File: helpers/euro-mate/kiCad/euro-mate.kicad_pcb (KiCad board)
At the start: 2 copper layers, 41 parts, among them J1 PWR, J10 OUT_2, J11 OUT_3, J12 OUT_4, J13 Conn_01x04, J14 Conn_01x04, J2 BB_TOP_RAIL, J2 PWR, J3 BB_BTM_RAIL, J5 JACK_1, J6 JACK_2, J7 JACK_3, J8 JACK_4, J9 OUT_1

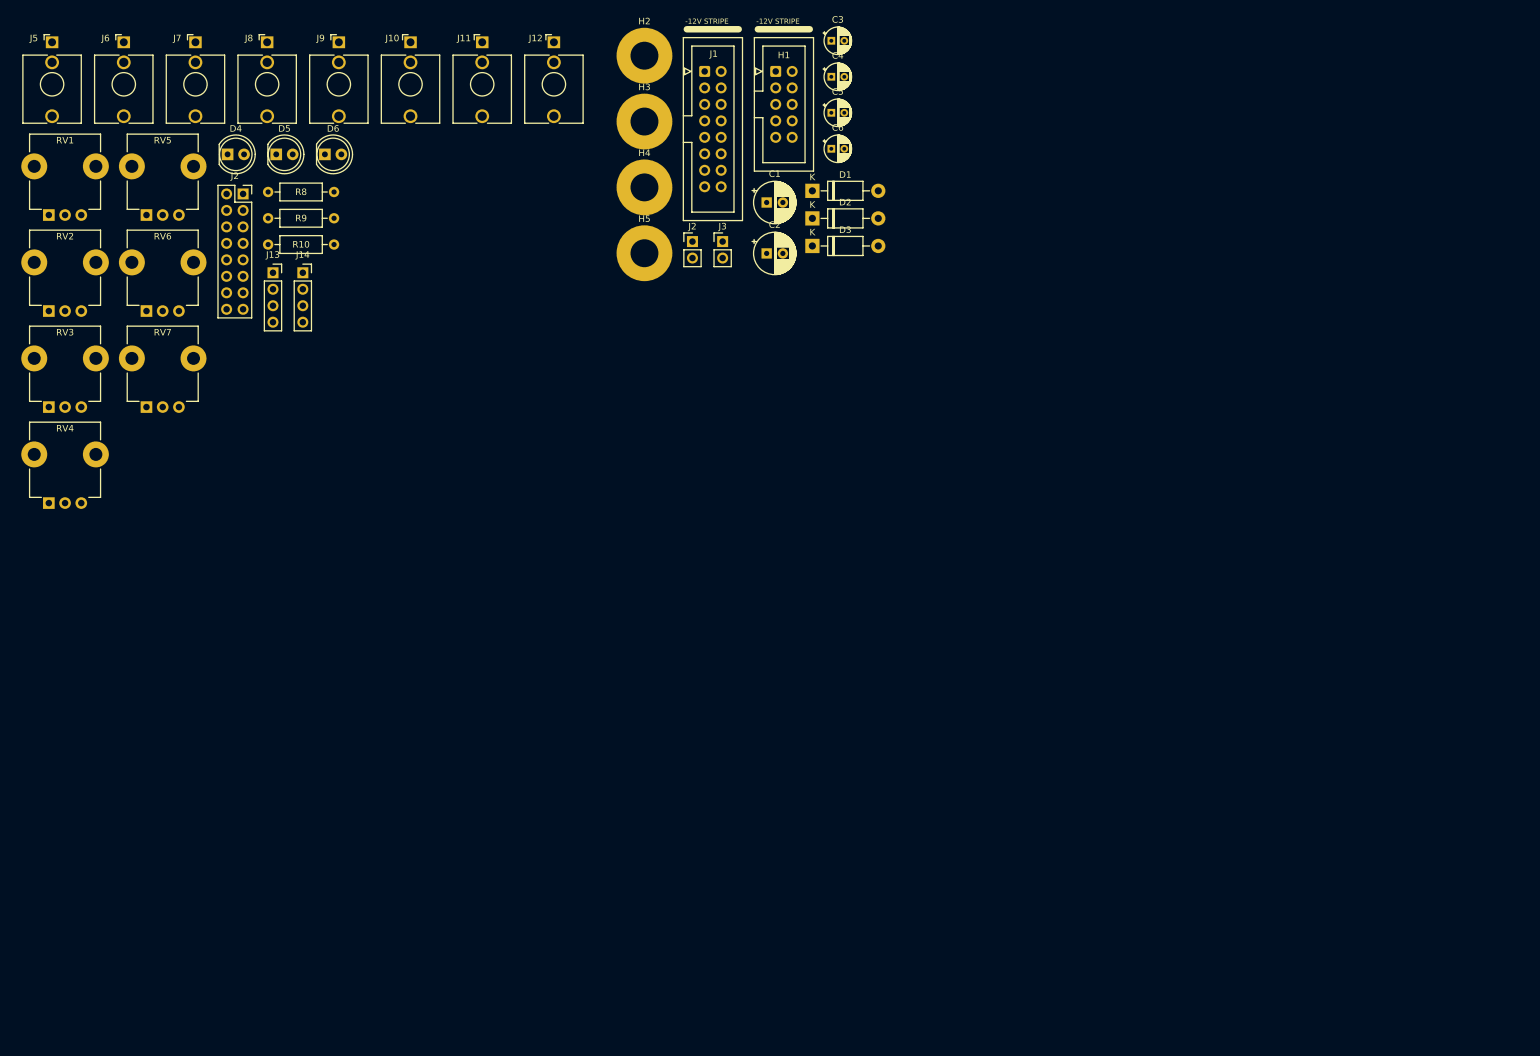
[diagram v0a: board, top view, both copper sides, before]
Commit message: update component status, add IBOM for built modules
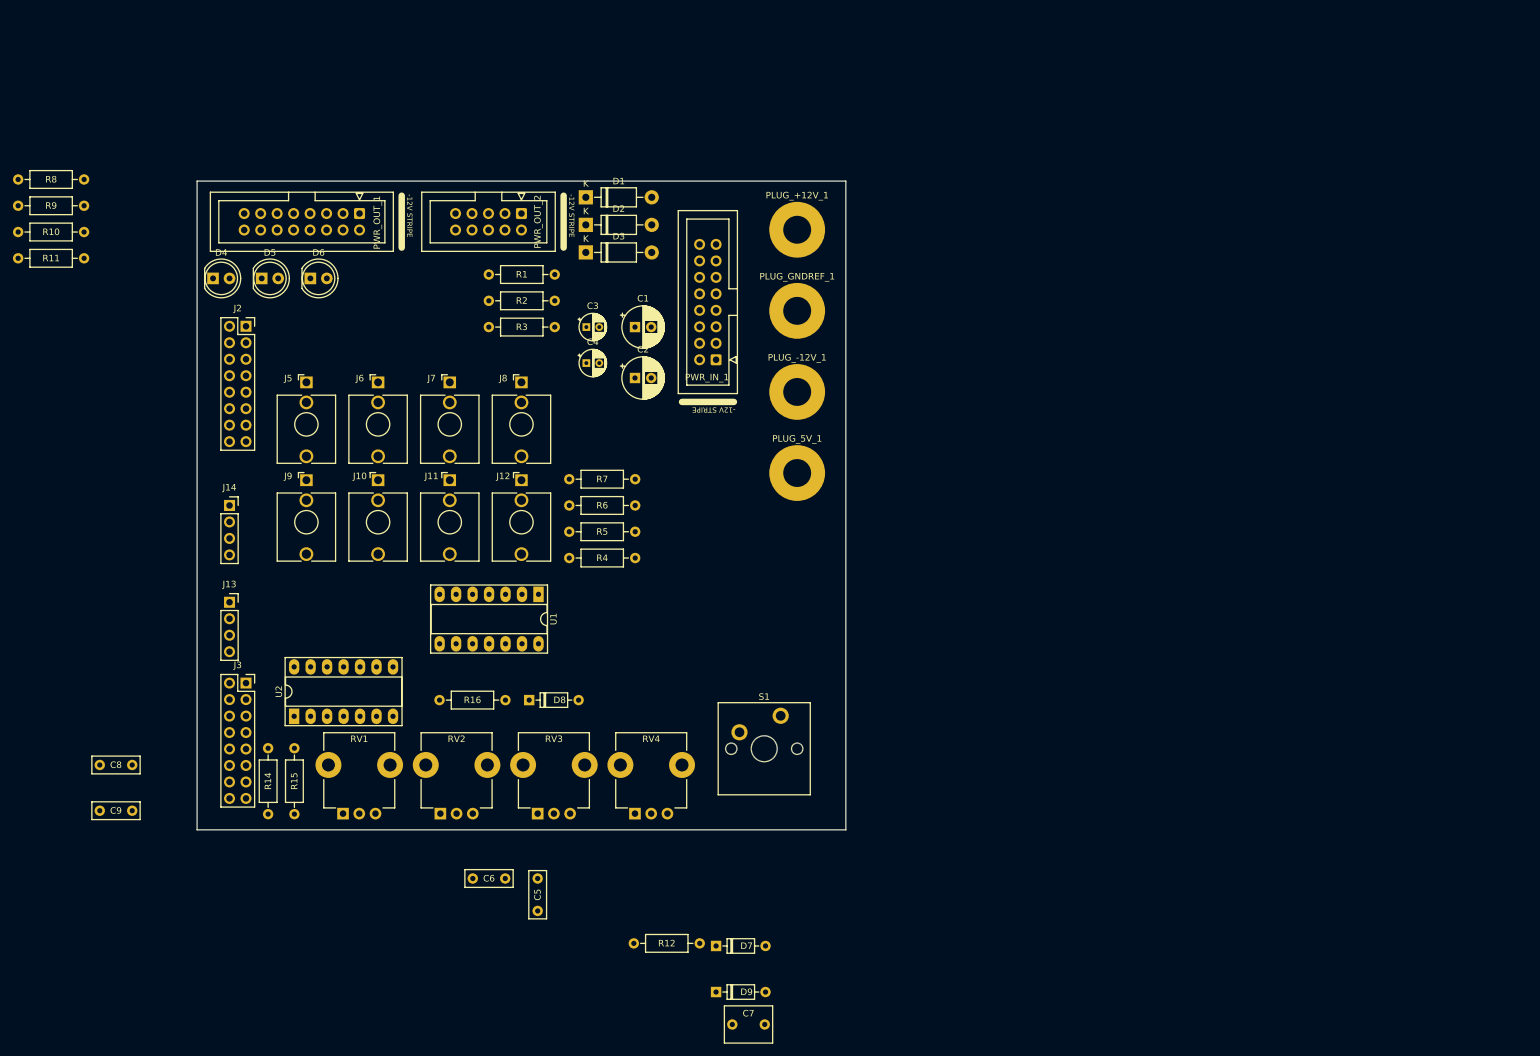
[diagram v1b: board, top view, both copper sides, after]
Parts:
- removed H1: Conn_02x05_PWR_Eurorack, Synth:IDC-Header_2x05_P2.54mm_Vertical
- removed H2, H3, H4, H5: MountingHole_Pad, MountingHole:MountingHole_4.3mm_M4_Pad
- removed J1: PWR, Synth:IDC-Header_2x08_P2.54mm_Vertical
- removed the J2 at (126.4, 59.3)
- removed the J2 at (57.1, 52.0)
- removed RV5, RV6: 1M, Synth:Potentiometer_TT_P0915N
- removed RV7: 100K, Synth:Potentiometer_TT_P0915N
- added C7: 1uF, Synth:C_RECT_MKT_1uF, F.Cu at (132.5, 180.0)
- added C8: 0.1uF, Synth:C_RECT_WIMA_0.1uF, F.Cu at (35.0, 140.0)
- added C9: 0.1uF, Synth:C_RECT_WIMA_0.1uF, F.Cu at (35.0, 147.1)
- added D7: 1N4148, Synth:D_DO-35_SOD27_P7.62mm_Horizontal, F.Cu at (130.0, 167.9)
- added D8: 1N4148, Synth:D_DO-35_SOD27_P7.62mm_Horizontal, F.Cu at (101.2, 130.0)
- added D9: 1N4148, Synth:D_DO-35_SOD27_P7.62mm_Horizontal, F.Cu at (130.0, 175.0)
- added J2: PWR, Connector_PinSocket_2.54mm:PinSocket_2x08_P2.54mm_Vertical, F.Cu at (57.5, 72.4)
- added PLUG_+12V_1: +12V, MountingHole:MountingHole_4.3mm_M4_Pad, F.Cu at (142.5, 57.5)
- added PLUG_-12V_1: -12V, MountingHole:MountingHole_4.3mm_M4_Pad, F.Cu at (142.5, 82.5)
- added PLUG_5V_1: +5V, MountingHole:MountingHole_4.3mm_M4_Pad, F.Cu at (142.5, 95.0)
- added PLUG_GNDREF_1: GNDREF, MountingHole:MountingHole_4.3mm_M4_Pad, F.Cu at (142.5, 70.0)
- added PWR_IN_1: PWR, Synth:IDC-Header_2x08_P2.54mm_Vertical, F.Cu at (130.0, 77.5)
- added PWR_OUT_1: PWR, Synth:IDC-Header_2x08_P2.54mm_Vertical, F.Cu at (75.0, 55.0)
- added PWR_OUT_2: Conn_02x05_PWR_Eurorack, Synth:IDC-Header_2x05_P2.54mm_Vertical, F.Cu at (100.0, 55.0)
- added R1: 10R, Synth:R_Default (DIN0207), F.Cu at (95.0, 64.4)
- added R11: 100K, Synth:R_Default (DIN0207), F.Cu at (22.4, 61.9)
- added R12: 47K, Synth:R_Default (DIN0207), F.Cu at (127.5, 167.5)
- added R14: 1K, Synth:R_Default (DIN0207), F.Cu at (61.0, 147.6)
- added R15: 100K, Synth:R_Default (DIN0207), F.Cu at (65.0, 147.6)
- added R16: 1K, Synth:R_Default (DIN0207), F.Cu at (97.5, 130.0)
- added R2: 10R, Synth:R_Default (DIN0207), F.Cu at (95.0, 68.5)
- added R3: 10R, Synth:R_Default (DIN0207), F.Cu at (95.0, 72.5)
- added R4: 1K, Synth:R_Default (DIN0207), F.Cu at (117.5, 108.1)
- added R5: 1K, Synth:R_Default (DIN0207), F.Cu at (117.5, 104.0)
- added R6: 1K, Synth:R_Default (DIN0207), F.Cu at (117.5, 100.0)
- added R7: 1K, Synth:R_Default (DIN0207), F.Cu at (117.5, 96.0)
- added S1: Keyswitch, PCM_Switch_Keyboard_Cherry_MX:SW_Cherry_MX_PCB_1.00u, F.Cu at (137.4, 137.5)
- added U1: TL074, Package_DIP:DIP-14_W7.62mm_Socket_LongPads, F.Cu at (102.6, 113.7)
- added U2: TL074, Package_DIP:DIP-14_W7.62mm_Socket_LongPads, F.Cu at (65.0, 132.5)
- C5, C6: footprint Capacitor_THT:CP_Radial_D4.0mm_P2.00mm -> Synth:C_RECT_WIMA_0.1uF
- J3: value BB_BTM_RAIL -> PWR; footprint Connector_PinHeader_2.54mm:PinHeader_1x02_P2.54mm_Vertical -> Connector_PinSocket_2.54mm:PinSocket_2x08_P2.54mm_Vertical
- RV1, RV2, RV3, RV4: value 100K -> B100K
- moved C5 126.4 mm to (102.5, 157.5), turned to -90 degrees
- moved C6 125.3 mm to (92.5, 157.5)
- moved RV1 102.8 mm to (75.0, 140.0)
- moved RV4 102.2 mm to (120.0, 140.0)
- moved J3 100.1 mm to (57.5, 127.4)
- moved RV2 98.2 mm to (90.0, 140.0)
- moved RV3 98.0 mm to (105.0, 140.0)
- moved J10 67.7 mm to (77.9, 102.6)
- moved J11 67.7 mm to (89.0, 102.6)
- moved J12 67.7 mm to (100.0, 102.6)
- moved J9 67.7 mm to (66.8, 102.6)
- moved J5 65.5 mm to (66.8, 87.5)
- moved J6 65.5 mm to (77.9, 87.5)
- moved J7 65.5 mm to (89.0, 87.5)
- moved J8 65.5 mm to (100.0, 87.5)
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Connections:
- C5 pad 1: +12V -> GNDREF
- C5 pad 2: GNDREF -> -12V
- C6 pad 1: GNDREF -> +12V
- C6 pad 2: -12V -> GNDREF
- J3 pad 1: -12V -> Net-(J3-Pin_1)
- J3 pad 2: GNDREF -> Net-(J3-Pin_2)
- RV1 pad 1: unconnected-(RV1-Pad1) -> GNDREF
- RV1 pad 2: unconnected-(RV1-Pad2) -> Net-(J3-Pin_15)
- RV1 pad 3: unconnected-(RV1-Pad3) -> +12V
- RV2 pad 1: unconnected-(RV2-Pad1) -> -12V
- RV2 pad 2: unconnected-(RV2-Pad2) -> Net-(J3-Pin_9)
- RV2 pad 3: unconnected-(RV2-Pad3) -> +12V
- RV3 pad 1: unconnected-(RV3-Pad1) -> -12V
- RV3 pad 2: unconnected-(RV3-Pad2) -> Net-(J3-Pin_11)
- RV3 pad 3: unconnected-(RV3-Pad3) -> +12V
- RV4 pad 1: unconnected-(RV4-Pad1) -> GNDREF
- RV4 pad 2: unconnected-(RV4-Pad2) -> Net-(J3-Pin_13)
- RV4 pad 3: unconnected-(RV4-Pad3) -> +12V
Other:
- board outline added: 100 x 100 mm

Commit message: 7555 readme
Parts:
- added 0402: R_0402, Resistors_SMD:R_0402, F.Cu at (145.2, 69.0)
- added 0603: R_0603, Resistors_SMD:R_0603, F.Cu at (145.2, 65.0)
- added 0805: R_0805, Resistors_SMD:R_0805, F.Cu at (140.8, 69.0)
- added 1206: R_1206, Resistors_SMD:R_1206, F.Cu at (140.8, 65.0)
- added C10: 0.1uF, Synth:C_RECT_WIMA_0.1uF, F.Cu at (87.8, 80.0)
- added C11: 0.1uF, Synth:C_RECT_WIMA_0.1uF, F.Cu at (102.2, 85.0)
- added C12: 10nF, Synth:C_RECT_WIMA_0.1uF, F.Cu at (139.4, 99.0)
- added C13: 0.1uF, Synth:C_RECT_WIMA_0.1uF, F.Cu at (157.0, 87.2)
- added C14: 0.1uF, Synth:C_RECT_WIMA_0.1uF, F.Cu at (142.8, 90.3)
- added D-PAK/TO-252: TO-252-3_TabPin2, TO_SOT_Packages_SMD:TO-252-3_TabPin2, F.Cu at (131.4, 66.5)
- added D10: LED, Synth:LED_D5.0mm (center Aligned), F.Cu at (242.0, 95.0)
- added H1: MountingHole, MountingHole:MountingHole_3.2mm_M3, F.Cu at (54.0, 54.0)
- added H2: MountingHole, MountingHole:MountingHole_3.2mm_M3, F.Cu at (54.0, 146.0)
- added H3: MountingHole, MountingHole:MountingHole_3.2mm_M3, F.Cu at (246.0, 54.0)
- added H4: MountingHole, MountingHole:MountingHole_3.2mm_M3, F.Cu at (246.0, 146.0)
- added HC49: Crystal_SMD_HC49-SD, Crystals:Crystal_SMD_HC49-SD, F.Cu at (117.0, 59.0)
- added J1: OUT_1, Synth:Jack_3.5mm_QingPu_WQP-PJ398SM_Vertical_CircularHoles, F.Cu at (65.0, 65.0)
- added J15: Conn_01x06_Socket, Connector_PinSocket_2.54mm:PinSocket_1x06_P2.54mm_Vertical, F.Cu at (59.5, 134.4)
- added J16: Conn_01x06_Socket, Connector_PinSocket_2.54mm:PinSocket_1x06_P2.54mm_Vertical, F.Cu at (59.5, 138.4)
- added J17: Conn_01x06_Socket, Connector_PinSocket_2.54mm:PinSocket_1x06_P2.54mm_Vertical, F.Cu at (87.3, 139.0)
- added J18: Conn_01x06_Socket, Connector_PinSocket_2.54mm:PinSocket_1x06_P2.54mm_Vertical, F.Cu at (103.7, 139.0)
- added J19: Conn_01x04, Connector_PinSocket_2.54mm:PinSocket_1x04_P2.54mm_Vertical, F.Cu at (175.1, 138.9)
- added J20: Conn_01x04, Connector_PinSocket_2.54mm:PinSocket_1x04_P2.54mm_Vertical, F.Cu at (220.0, 139.1)
- added J21: Conn_01x04, Connector_PinSocket_2.54mm:PinSocket_1x04_P2.54mm_Vertical, F.Cu at (240.0, 139.1)
- added J22: Conn_01x04, Connector_PinSocket_2.54mm:PinSocket_1x04_P2.54mm_Vertical, F.Cu at (230.0, 139.1)
- added J23: Conn_01x04, Connector_PinSocket_2.54mm:PinSocket_1x04_P2.54mm_Vertical, F.Cu at (210.0, 139.1)
- added J24: Conn_01x02_Socket, Synth:PinSocket_1x02_P2.54mm_Vertical, F.Cu at (155.8, 139.2)
- added J4: OUT_4, Synth:Jack_3.5mm_QingPu_WQP-PJ398SM_Vertical_CircularHoles, F.Cu at (65.0, 98.0)
- added QFN28: QFN-28-1EP_4x4mm_Pitch0.4mm, Housings_DFN_QFN:QFN-28-1EP_4x4mm_Pitch0.4mm, F.Cu at (107.0, 54.2)
- added R13: 100K, Synth:R_Default (DIN0207), F.Cu at (139.4, 106.0)
- added R17: 1K, Synth:R_Default (DIN0207), F.Cu at (196.1, 139.2)
- added R18: 470R, Synth:R_Default (DIN0207), F.Cu at (203.9, 100.0)
- added R19: 680R, Synth:R_Default (DIN0207), F.Cu at (217.0, 100.0)
- added R20: 680R, Synth:R_Default (DIN0207), F.Cu at (236.9, 100.0)
- added REF**: Resistor_Table_small, PCBRulers:Resistor_Table_small, F.Cu at (124.0, 93.5)
- added REF**: Voltage Divider, PCBRulers:Voltage_Divider, F.Cu at (112.8, 85.2)
- added REF**: Drills, PCBRulers:Drills, F.Cu at (232.9, 105.5)
- added RV5: 100K, Synth:Potentiometer_TT_P0915N, F.Cu at (110.0, 125.0)
- added RV6: 100K, Synth:Potentiometer_TT_P0915N, F.Cu at (110.0, 105.0)
- added S2: Keyswitch, PCM_Switch_Keyboard_Cherry_MX:SW_Cherry_MX_PCB_1.00u, F.Cu at (191.0, 125.0)
- added SC70/: SOT-323_SC-70, TO_SOT_Packages_SMD:SOT-323_SC-70, F.Cu at (117.3, 54.0)
- added SMA: D_SMA, Diodes_SMD:D_SMA, F.Cu at (98.3, 53.0)
- added SMB: D_SMB, Diodes_SMD:D_SMB, F.Cu at (98.3, 59.0)
- added SOD323: D_SOD-323, Diodes_SMD:D_SOD-323, F.Cu at (150.5, 66.0)
- added SOIC8: SOIC-8_3.9x4.9mm_Pitch1.27mm, Housings_SOIC:SOIC-8_3.9x4.9mm_Pitch1.27mm, F.Cu at (98.3, 64.6)
- added SOT223: SOT-223, TO_SOT_Packages_SMD:SOT-223, F.Cu at (120.3, 66.6)
- added SOT23: SOT-23, TO_SOT_Packages_SMD:SOT-23, F.Cu at (92.0, 53.0)
- added SOT23-5: SOT-23-5, TO_SOT_Packages_SMD:SOT-23-5, F.Cu at (86.7, 53.0)
- added SOT89: SOT-89-3, TO_SOT_Packages_SMD:SOT-89-3, F.Cu at (113.3, 65.0)
- added TQFP32: TQFP-32_7x7mm_Pitch0.8mm, Housings_QFP:TQFP-32_7x7mm_Pitch0.8mm, F.Cu at (78.1, 56.1)
- added TSSOP: TSSOP-16_4.4x5mm_Pitch0.65mm, Housings_SSOP:TSSOP-16_4.4x5mm_Pitch0.65mm, F.Cu at (106.7, 62.0)
- added U3: TL072, Package_DIP:DIP-8_W7.62mm_Socket_LongPads, F.Cu at (146.0, 87.4)
- added WS2812: LED_WS2812-PLCC6, LEDs:LED_WS2812-PLCC6, F.Cu at (89.5, 59.4)
- C1: value 47uF -> 0.1uF; footprint Capacitor_THT:CP_Radial_D6.3mm_P2.50mm -> Capacitor_THT:CP_Radial_D4.0mm_P2.00mm
- C3, C4: value 0.1uF -> 47uF; footprint Capacitor_THT:CP_Radial_D4.0mm_P2.00mm -> Capacitor_THT:CP_Radial_D6.3mm_P2.50mm
- C5, C6: footprint Synth:C_RECT_WIMA_0.1uF -> Capacitor_THT:CP_Radial_D4.0mm_P2.00mm
- C7: value 1uF -> 0.1uF; footprint Synth:C_RECT_MKT_1uF -> Synth:C_RECT_WIMA_0.1uF
- C9: value 0.1uF -> 10nF
- D4, D5, D6: value LED -> 1N4148; footprint Synth:LED_D5.0mm (center Aligned) -> Synth:D_DO-35_SOD27_P7.62mm_Horizontal
- D8, D9: value 1N4148 -> LED; footprint Synth:D_DO-35_SOD27_P7.62mm_Horizontal -> Synth:LED_D5.0mm (center Aligned)
- J10: value OUT_2 -> JACK_2
- J11: value OUT_3 -> JACK_3
- J12: value OUT_4 -> JACK_4
- J14: value Conn_01x04 -> Conn_01x06_Pin; footprint Connector_PinSocket_2.54mm:PinSocket_1x04_P2.54mm_Vertical -> Connector_PinHeader_2.54mm:PinHeader_1x06_P2.54mm_Vertical
- J2: value PWR -> OUT_2; footprint Connector_PinSocket_2.54mm:PinSocket_2x08_P2.54mm_Vertical -> Synth:Jack_3.5mm_QingPu_WQP-PJ398SM_Vertical_CircularHoles
- J3: value PWR -> OUT_3; footprint Connector_PinSocket_2.54mm:PinSocket_2x08_P2.54mm_Vertical -> Synth:Jack_3.5mm_QingPu_WQP-PJ398SM_Vertical_CircularHoles
- J5: value JACK_1 -> Conn_01x04; footprint Synth:Jack_3.5mm_QingPu_WQP-PJ398SM_Vertical_CircularHoles -> Connector_PinSocket_2.54mm:PinSocket_1x04_P2.54mm_Vertical
- J6: value JACK_2 -> Conn_01x06_Socket; footprint Synth:Jack_3.5mm_QingPu_WQP-PJ398SM_Vertical_CircularHoles -> Connector_PinSocket_2.54mm:PinSocket_1x06_P2.54mm_Vertical
- J7: value JACK_3 -> Conn_01x06_Pin; footprint Synth:Jack_3.5mm_QingPu_WQP-PJ398SM_Vertical_CircularHoles -> Connector_PinHeader_2.54mm:PinHeader_1x06_P2.54mm_Vertical
- J8: value JACK_4 -> Conn_01x06_Socket; footprint Synth:Jack_3.5mm_QingPu_WQP-PJ398SM_Vertical_CircularHoles -> Connector_PinSocket_2.54mm:PinSocket_1x06_P2.54mm_Vertical
- J9: value OUT_1 -> JACK_1
- R1, R2, R3: value 10R -> 1K
- R10: value 1K -> 39K
- R11: value 100K -> 39K
- R12: value 47K -> 100K
- R14: value 1K -> 33K
- R15: value 100K -> 33K
- R5, R6, R7: value 1K -> 10R
- R8: value 470R -> 1M
- R9: value 1K -> 1M
- RV1, RV2, RV3, RV4: value B100K -> 100K
- moved C6 152.2 mm to (228.8, 89.8), turned to -90 degrees
- moved C5 146.7 mm to (228.8, 82.8)
- moved R10 140.8 mm to (151.9, 113.0)
- moved R11 135.7 mm to (151.9, 102.5)
- moved D3 135.4 mm to (244.0, 80.0), turned to -90 degrees
- moved R8 133.0 mm to (139.4, 113.0)
- moved R9 126.7 mm to (139.4, 102.5)
- moved C3 125.9 mm to (234.8, 89.8), turned to -90 degrees
- moved R7 123.4 mm to (240.8, 90.4), turned to 90 degrees
- moved D9 121.2 mm to (221.0, 95.0), turned to -90 degrees
- moved C2 117.3 mm to (234.8, 82.2), turned to -90 degrees
- moved D2 115.0 mm to (220.0, 90.0), turned to 90 degrees
- moved D8 113.3 mm to (209.0, 95.0), turned to -90 degrees
- moved D4 110.7 mm to (151.9, 116.0)
- moved D6 109.4 mm to (173.0, 98.0), turned to 180 degrees
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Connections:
- C1 pad 1: +12V -> +5V
- C2 pad 1: GNDREF -> +12V
- C2 pad 2: -12V -> GNDREF
- C3 pad 1: +12V -> GNDREF
- C3 pad 2: GNDREF -> -12V
- C4 pad 1: GNDREF -> +5V
- C4 pad 2: -12V -> GNDREF
- C5 pad 1: GNDREF -> +12V
- C5 pad 2: -12V -> GNDREF
- C6 pad 1: +12V -> GNDREF
- C6 pad 2: GNDREF -> -12V
- C7 pad 1: Net-(D9-K) -> +12V
- C7 pad 2: Net-(D7-K) -> GNDREF
- C8 pad 1: +12V -> GNDREF
- C8 pad 2: GNDREF -> -12V
- C9 pad 1: GNDREF -> Net-(J24-Pin_2)
- C9 pad 2: -12V -> Net-(D4-K)
- D4 pad 1: GNDREF -> Net-(D4-K)
- D4 pad 2: Net-(D4-A) -> GNDREF
- D5 pad 1: GNDREF -> Net-(D5-K)
- D5 pad 2: Net-(D5-A) -> GNDREF
- D6 pad 2: -12V -> Net-(D6-A)
- D7 pad 2: GNDREF -> Net-(D7-A)
- D8 pad 1: Net-(D8-K) -> GNDREF
- D9 pad 1: Net-(D9-K) -> GNDREF
- J10 pad T: Net-(J10-PadT) -> Net-(J13-Pin_2)
- J11 pad T: Net-(J11-PadT) -> Net-(J13-Pin_3)
- J12 pad T: Net-(J12-PadT) -> Net-(J13-Pin_4)
- J9 pad T: Net-(J9-PadT) -> Net-(J13-Pin_1)
- PLUG_+12V_1 pad 1: Net-(D1-A) -> Net-(D2-A)
- PLUG_-12V_1 pad 1: Net-(D2-K) -> Net-(D3-K)
- PLUG_5V_1 pad 1: Net-(D3-A) -> Net-(D1-A)
- PWR_IN_1 pad 1: Net-(D2-K) -> Net-(D3-K)
- PWR_IN_1 pad 10: Net-(D1-A) -> Net-(D2-A)
- PWR_IN_1 pad 11: Net-(D3-A) -> Net-(D1-A)
- PWR_IN_1 pad 12: Net-(D3-A) -> Net-(D1-A)
- PWR_IN_1 pad 13: Net-(J3-Pin_14) -> unconnected-(PWR_IN_1-CV-Pad13)
- PWR_IN_1 pad 14: Net-(J3-Pin_14) -> unconnected-(PWR_IN_1-CV-Pad14)
- PWR_IN_1 pad 15: Net-(J3-Pin_16) -> unconnected-(PWR_IN_1-GATE-Pad15)
- PWR_IN_1 pad 16: Net-(J3-Pin_16) -> unconnected-(PWR_IN_1-GATE-Pad16)
- PWR_IN_1 pad 2: Net-(D2-K) -> Net-(D3-K)
- PWR_IN_1 pad 9: Net-(D1-A) -> Net-(D2-A)
- PWR_OUT_2 pad 1: +12V -> -12V
- PWR_OUT_2 pad 10: -12V -> +12V
- PWR_OUT_2 pad 2: +12V -> -12V
- PWR_OUT_2 pad 9: -12V -> +12V
- R1 pad 1: +12V -> Net-(U1A--)
- R1 pad 2: Net-(D1-K) -> Net-(J1-PadT)
- R10 pad 1: GNDREF -> Net-(D4-K)
- R10 pad 2: Net-(D6-K) -> GNDREF
- R11 pad 1: Net-(U2A-+) -> Net-(D5-K)
- R12 pad 1: Net-(D7-K) -> +12V
- R12 pad 2: Net-(U2A-+) -> Net-(U3A--)
- R14 pad 1: Net-(U2A--) -> Net-(U3A--)
- R15 pad 1: +12V -> Net-(U3B--)
- R15 pad 2: Net-(U2A--) -> GNDREF
- R16 pad 1: Net-(D8-K) -> Net-(R16-Pad1)
- R16 pad 2: Net-(J3-Pin_12) -> Net-(J19-Pin_1)
- R2 pad 1: -12V -> Net-(U1B--)
- R2 pad 2: Net-(D2-A) -> Net-(J2-PadT)
- R3 pad 1: +5V -> Net-(U1C--)
- R3 pad 2: Net-(D3-K) -> Net-(J3-PadT)
- R4 pad 1: Net-(U1A--) -> Net-(U1D--)
- R4 pad 2: Net-(J9-PadT) -> Net-(J4-PadT)
- R5 pad 1: Net-(U1B--) -> +5V
- R5 pad 2: Net-(J10-PadT) -> Net-(D1-K)
- R6 pad 1: Net-(U1C--) -> +12V
- R6 pad 2: Net-(J11-PadT) -> Net-(D2-K)
- R7 pad 1: Net-(U1D--) -> -12V
- R7 pad 2: Net-(J12-PadT) -> Net-(D3-A)
- R8 pad 1: +5V -> Net-(J24-Pin_2)
- R8 pad 2: Net-(D4-A) -> GNDREF
- R9 pad 1: +12V -> Net-(J24-Pin_1)
- R9 pad 2: Net-(D5-A) -> GNDREF
- RV1 pad 1: GNDREF -> Net-(J17-Pin_4)
- RV1 pad 2: Net-(J3-Pin_15) -> Net-(J17-Pin_5)
- RV1 pad 3: +12V -> Net-(J17-Pin_6)
- RV2 pad 1: -12V -> Net-(J17-Pin_1)
- RV2 pad 2: Net-(J3-Pin_9) -> Net-(J17-Pin_2)
- RV2 pad 3: +12V -> Net-(J17-Pin_3)
- RV3 pad 1: -12V -> GNDREF
- RV3 pad 2: Net-(J3-Pin_11) -> Net-(R16-Pad1)
- RV3 pad 3: +12V -> Net-(D6-K)
- RV4 pad 2: Net-(J3-Pin_13) -> Net-(R17-Pad1)
- RV4 pad 3: +12V -> Net-(D7-K)
- S1 pad 2: Net-(D9-A) -> Net-(J24-Pin_2)
- U1 pad 10: Net-(J13-Pin_3) -> Net-(J5-Pin_3)
- U1 pad 12: Net-(J13-Pin_4) -> Net-(J5-Pin_4)
- U1 pad 3: Net-(J13-Pin_1) -> Net-(J5-Pin_1)
- U1 pad 5: Net-(J13-Pin_2) -> Net-(J5-Pin_2)
- U2 pad 1: Net-(D8-A) -> Net-(J6-Pin_1)
- U2 pad 10: Net-(J3-Pin_8) -> Net-(J14-Pin_3)
- U2 pad 12: Net-(J3-Pin_1) -> Net-(J14-Pin_4)
- U2 pad 13: Net-(J3-Pin_2) -> Net-(J14-Pin_5)
- U2 pad 14: Net-(J3-Pin_4) -> Net-(J14-Pin_6)
- U2 pad 2: Net-(U2A--) -> Net-(J6-Pin_2)
- U2 pad 3: Net-(U2A-+) -> Net-(J6-Pin_3)
- U2 pad 5: Net-(J3-Pin_7) -> Net-(J6-Pin_4)
- U2 pad 6: Net-(J3-Pin_5) -> Net-(J6-Pin_5)
- U2 pad 7: Net-(J3-Pin_3) -> Net-(J6-Pin_6)
- U2 pad 8: Net-(J3-Pin_6) -> Net-(J14-Pin_1)
- U2 pad 9: Net-(J3-Pin_10) -> Net-(J14-Pin_2)
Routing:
- net +12V: track 0.00 -> 500.0 mm, vias 0 -> 2
- net -12V: track 0.00 -> 364.0 mm
- net +5V: track 0.00 -> 132.0 mm
- net Net-(J24-Pin_1): track 0.00 -> 131.6 mm, vias 0 -> 1
- net Net-(J24-Pin_2): track 0.00 -> 68.2 mm
- net Net-(U1B--): track 0.00 -> 43.3 mm
- net Net-(U1D--): track 0.00 -> 39.3 mm
- net Net-(J5-Pin_4): track 0.00 -> 35.9 mm
- net Net-(D7-A): track 0.00 -> 35.1 mm
- net Net-(D4-K): track 0.00 -> 34.0 mm
- net Net-(R16-Pad1): track 0.00 -> 30.5 mm
- net Net-(J18-Pin_3): track 0.00 -> 30.1 mm
- net Net-(J17-Pin_3): track 0.00 -> 30.0 mm
- net Net-(D1-A): track 0.00 -> 29.9 mm
- net Net-(D3-K): track 0.00 -> 29.4 mm
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- added copper zone on B.Cu, net GNDREF
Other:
- board size 100 x 100 mm -> 200 x 100 mm
- board text added: "+12V"
- board text added: "+5V"
- board text added: "-12V"
- board text added: "1in=2.54cm 1cm≈0.394in 1mil=1/1000in 1mil=25,4µm"
- board text added: "7x7mm 0.7mm"
- board text added: "A"
- board text added: "A+"
- board text added: "A-"
- board text added: "B"
- board text added: "B+"
- board text added: "B-"
- board text added: "C"
- board text added: "C+"
- board text added: "C-"
- board text added: "D"
- board text added: "D+"
- board text added: "D-"
- board text added: "EURO MATE"
- board text added: "GNDREF"
- board text added: "Gate #1"
- board text added: "Gate #2"
- board text added: "Jack #1"
- board text added: "Jack #2"
- board text added: "Jack #3"
- board text added: "Jack #4"
- board text added: "MASTER CLOCK"
- board text added: "OUT #1"
- board text added: "OUT #2"
- board text added: "OUT #3"
- board text added: "OUT #4"
- board text added: "POT #1"
- board text added: "POT #2"
- board text added: "POT #3"
- board text added: "POT #4"
- board text added: "Resistor: U=R*I Capacitor: C=Q/U Coil: U=L*dI/dt"
- board text added: "SOT323"
- board text added: "TRIG #1"
- board text added: "TRIG #2"
- board text added: "unused op-amp"

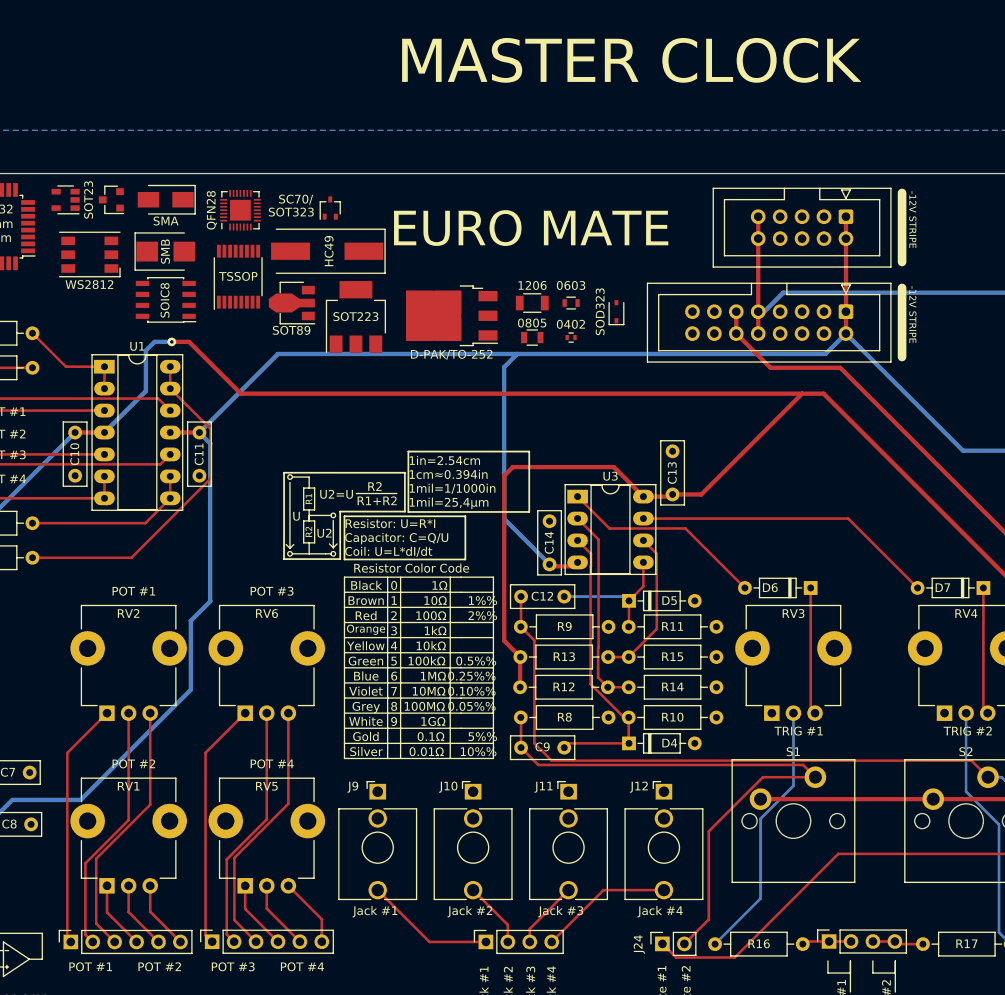
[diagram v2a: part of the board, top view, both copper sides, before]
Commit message: finish up PCB finals for run-2, continue on C code for midas/sequencer
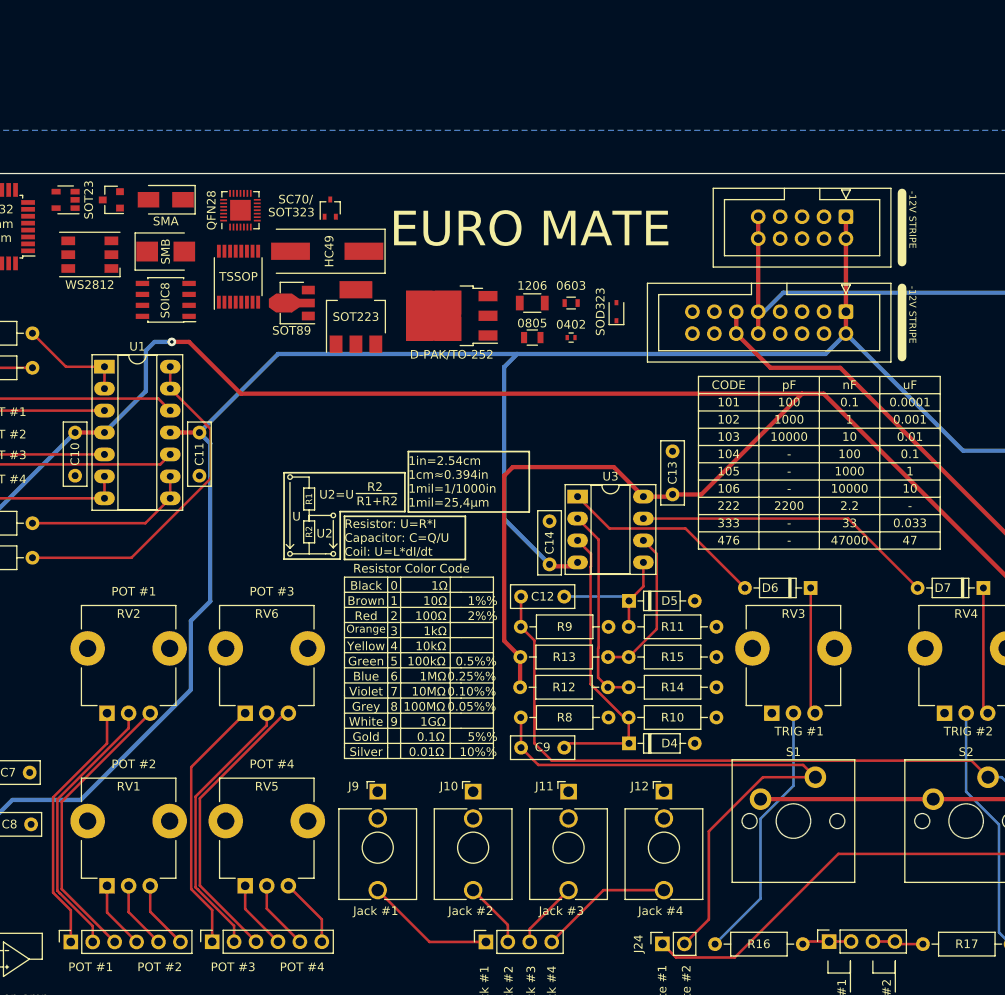
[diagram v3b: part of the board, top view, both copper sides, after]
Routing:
- net Net-(J18-Pin_3): track 30.1 -> 33.6 mm
- net Net-(J17-Pin_3): track 30.0 -> 33.3 mm
- net Net-(J18-Pin_2): track 28.7 -> 31.7 mm
- net Net-(J17-Pin_2): track 28.9 -> 31.6 mm
- net Net-(J17-Pin_1): track 28.6 -> 29.9 mm
- net Net-(J18-Pin_1): track 28.7 -> 30.1 mm
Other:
- board text added: "-"
- board text added: "0.0001"
- board text added: "0.001"
- board text added: "0.01"
- board text added: "0.033"
- board text added: "0.1"
- board text added: "1"
- board text added: "10"
- board text added: "100"
- board text added: "1000"
- board text added: "10000"
- board text added: "101"
- board text added: "102"
- board text added: "103"
- board text added: "104"
- board text added: "105"
- board text added: "106"
- board text added: "2.2"
- board text added: "2200"
- board text added: "222"
- board text added: "33"
- board text added: "333"
- board text added: "47"
- board text added: "47000"
- board text added: "476"
- board text added: "CODE"
- board text added: "nF"
- board text added: "pF"
- board text added: "uF"
- board text removed: "MASTER CLOCK"
